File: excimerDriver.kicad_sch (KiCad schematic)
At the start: 37 parts, among them IC3 INA210, IC6 STM32G071KBT6, J1 B08B-XASK-1-A_LF__SN_, J2 TC2050-IDC, J3 BM02B-SRSS-TB_LF__SN_, J4 BM02B-SRSS-TB_LF__SN_, J6 640445-2, Q3 BSS138

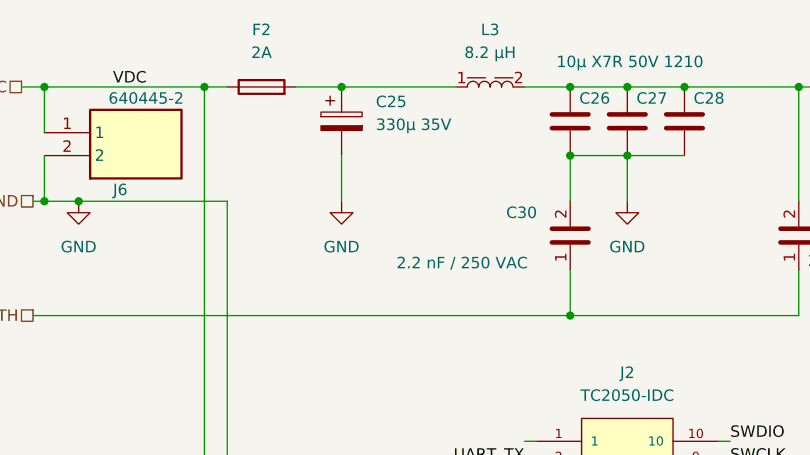
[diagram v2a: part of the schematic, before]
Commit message: branch main, transfomer changed to EF25
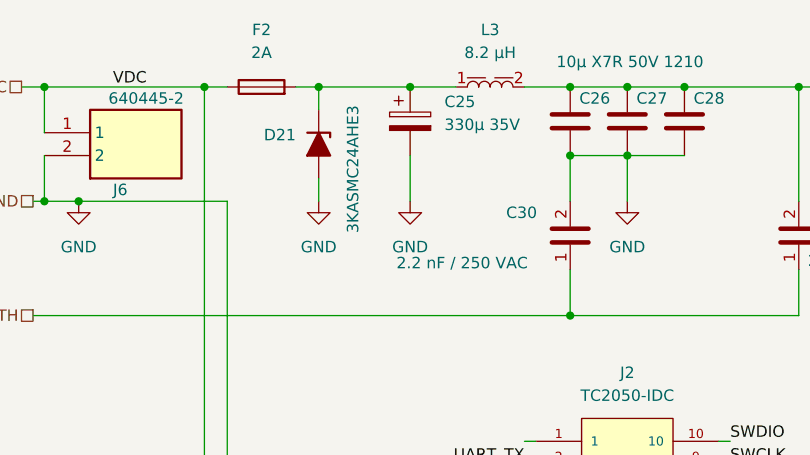
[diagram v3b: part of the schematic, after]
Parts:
- added D21: 3KASMC24AHE3, Diode_SMD:D_SMC, symbol Device:D_Zener_Filled
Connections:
- net GND: now also D21.2 (A)
- net at C25.1, F2.2, L3.1: now also D21.1 (K)
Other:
- moved on the sheet: C25
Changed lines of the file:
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@@
 	)
 	(junction
-		(at 57.15 25.4)
-		(diameter 0)
-		(color 0 0 0 0)
-	)
-	(junction
 		(at 107.95 25.4)
 		(diameter 0)
@@
 	)
 	(junction
+		(at 54.61 25.4)
+		(diameter 0)
+		(color 0 0 0 0)
+	)
+	(junction
+		(at 64.77 25.4)
+		(diameter 0)
+		(color 0 0 0 0)
+	)
+	(junction
 		(at 82.55 50.8)
 		(diameter 0)
@@
 	(wire
 		(pts
+			(xy 54.61 25.4) (xy 64.77 25.4)
+		)
+		(stroke
+			(width 0)
+			(type default)
+		)
+	)
+	(wire
+		(pts
 			(xy 236.22 130.81) (xy 223.52 130.81)
 		)
@@
 	(wire
 		(pts
-			(xy 52.07 25.4) (xy 57.15 25.4)
+			(xy 52.07 25.4) (xy 54.61 25.4)
 		)
 		(stroke
@@
 	(wire
 		(pts
+			(xy 54.61 25.4) (xy 54.61 27.94)
+		)
+		(stroke
+			(width 0)
+			(type default)
+		)
+	)
+	(wire
+		(pts
 			(xy 157.48 130.81) (xy 161.29 130.81)
 		)
@@
 	(wire
 		(pts
-			(xy 57.15 25.4) (xy 69.85 25.4)
+			(xy 99.06 67.31) (xy 116.84 67.31)
 		)
 		(stroke
@@
 	(wire
 		(pts
-			(xy 99.06 67.31) (xy 116.84 67.31)
+			(xy 95.25 101.6) (xy 95.25 104.14)
 		)
 		(stroke
@@
 	(wire
 		(pts
-			(xy 95.25 101.6) (xy 95.25 104.14)
+			(xy 31.75 132.08) (xy 48.26 132.08)
 		)
 		(stroke
@@
 	(wire
 		(pts
-			(xy 31.75 132.08) (xy 48.26 132.08)
+			(xy 107.95 38.1) (xy 107.95 25.4)
 		)
 		(stroke
@@
 	(wire
 		(pts
-			(xy 107.95 38.1) (xy 107.95 25.4)
+			(xy 64.77 25.4) (xy 69.85 25.4)
 		)
 		(stroke
@@
 	(wire
 		(pts
-			(xy 57.15 38.1) (xy 57.15 33.02)
+			(xy 64.77 33.02) (xy 64.77 38.1)
 		)
 		(stroke
@@
 	(wire
 		(pts
+			(xy 54.61 35.56) (xy 54.61 38.1)
+		)
+		(stroke
+			(width 0)
+			(type default)
+		)
+	)
+	(wire
+		(pts
 			(xy 48.26 132.08) (xy 48.26 114.3)
 		)
@@
 			"AAD4/////////yhzMtMiAQAA+P////////8EAAAAIgEAAPj/////////BAAAACIBAAD4////////"
 			"/yhzMtMiAQAA+P////////8EAAAAIgEAAPj/////////KHMy0yIBAAD4/////////yhzMtMiAQAA"
-			"+P////////8EAAAAIgEAAA=="
+			"+P////////8EAAAAIgEAAGaKDD5DdIJB3WLewGaKDD4AAACAAAAAAAAAgL8AAAAAAAAAAAAAAAAA"
+			"AAAAAAAAAAAAAAD///////////////8AAAAAAAAAgGaKDD4CAAAA5TYdQI+ERMAAAACA5TYdwAAA"
+			"AAAAAAAAe/I+Fd4MAYDgjqtF/n8AADsPhUECXNHAZYoMPhmwhkHLbdDAZ4oMPqrfhUHm5NDAZooM"
+			"PgUAAAAgJvNF/n8AACBwzrXeAQAAAAAAAN4BAAA+/FYnLr07swAAgL/trYknLr07swAAgL/trYkn"
+			"Lr07swAAgL8YsIZBzG3QwGaKDD48D4VBzG3QwGaKDD48D4VBAVzRwGaKDD4AAACAAAAAAP//f78A"
+			"AAAAAAAAAAAAAAAAAAAAAAAAAAAAAAD///////////////8AAAAAAAAAgGaKDD4CAAAAno8JQrQ2"
+			"ncAAAACAno8JwsB5EfveAQAACvJNFd4NAYDgjqtF/n8AAEJ0gkHeYt7AZYoMPj0PhUEAXNHAZ4oM"
+			"PsDBg0Fv39fAZooMPgUAAAAgJvNF/n8AACBwzrXeAQAAAAAAAAAAAADtrYknLr07swAAgL9JbIkn"
+			"Lr07swAAgL9NTIonLr07swAAgL88D4VBAVzRwGaKDD5DdIJB3WLewGaKDD48D4VB3WLewGaKDD4A"
+			"AAAAAAAAgAAAgL8AAAAAAAAAAAAAAAAAAAAAAAAAAAAAAAD///////////////8AAACAAAAAAGaK"
+			"DD4CAAAAAAAAgI+ERMCPhERA5TYdwAAAAAAAAAAAGfJcFQAOAYDgjqtF/n8AAGDEfkECXNHAp8y5"
+			"PfKCf0HLbdDAZ4oMPqkjf0Hm5NDAunDpPQUAAAAgJvNF/n8AACBwzrXeAQAAAAAAAN4BAADzBDU/"
+			"YsAEM/MENb/zBDU/Y8AEM/MENb/zBDU/YsAEM/MENb/xgn9BzG3QwGaKDD5hxH5BzG3QwKjMuT1h"
+			"xH5BAVzRwKjMuT0VBTU/AAAAANEENb8AAAAAAAAAAAAAAAAAAAAAAAAAAAAAAAD/////////////"
+			"//8AAAAAn/9/v8lQfUEAAAAA/vOrwZ6PCUKejwnCAAAAgOB5EfveAQAAKPJjFd4PAYDgjqtF/n8A"
+			"AGDEfkECXNHAp8y5PfKCf0HLbdDAZ4oMPqkjf0Hm5NDAunDpPQUAAAAgJvNF/n8AACBwzrXeAQAA"
+			"AAAAAAAAAADzBDU/YsAEM/MENb/zBDU/YsAEM/MENb/zBDU/YsAEM/MENb/xgn9BzG3QwGaKDD5h"
+			"xH5BAVzRwKjMuT3xgn9BAVzRwGaKDD4VBTU/AAAAANEENb8AAAAAAAAAAAAAAAAAAAAAAAAAAAAA"
+			"AAD///////////////8AAAAAAAAAAAAAAAAAAAAAAAAAAAAAAAAAAAAAAAAAAAAAAAAAAAAAAAAA"
+			"AAAAAAAAAAAAAAAAAAAAAAAAAAAAAAAAAAAAAAAAAAAAAAAAAAAAAAAAAAAAAAAAAAAAAAAAAAAA"
+			"AAAAAAAAAAAAAAAAAAAAAAAAAAAAAAAAAAAAAAAAAAAAAAAAAAAAAAAAAAAAAAAAAAAAAAAAAAAA"
+			"AAAAAAAAAAAAAAAAAAAAAAAAAAAAAAAAAAAAAAAAAAAAAAAAAAAAAAAAAAAAAAAAAAAAAAAAAAAA"
+			"AAAAAAAAAAAAAAAAAAAAAAAAAAAAAAAAAAAAAAAAAAAAAAAAAAAAAAAAAAAAAAAAAAAAAAAAAAAA"
+			"AAAAAAAAAAAAAAAAAAAAAAAAAAAAAAAAAAAAAAAAAAAAAAAAAAAAAAAAAAAAAAAAAAAAAAAAAAAA"
+			"AAAAAAAAAAAAAAAAAAAAAAAAAAAAAAAAAAAAAAAAAAAAAAAAAAAAAAAAAAAAAAAAAAAAAAAAAAAA"
+			"AAAAAAAAAAAAAAAAAAAAAAAAAAAAAAAAAAAAAAAAAAAAAAAAAAAAAAAAAAAAAAAAAAAAAAAAAAAA"
+			"AAAAAAAAAAAAAAAAAAAAAAAAAAAAAAAAAAAAAAAAAAAAAAAAAAAAAAAAAAAAAAAAAAAAAAAAAAAA"
+			"AAAAAAAAAAAAAAAAAAAAAAAAAAAAAAAAAAAAAAAAAAAAAAAAAAAAAAAAAAAAAAAAAAAAAAAAAAAA"
+			"AAAAAAAAAAAAAAAAAAAAAAAAAAAAAAAAAAAAAAAAAAAAAAAAAAAAAAAAAAAAAAAAAAAAAAAAAAAA"
+			"AAAAAAAAAAAAAAAAAAAAAAAAAAAAAAAAAAAAAAAAAAAAAAAAAAAAAAAAAAAAAAAAAAAAAAAAAAAA"
+			"AAAAAAAAAAAAAAAAAAAAAAAAAAAAAAAAAAAAAAAAAAAAAAAAAAAAAAAAAAAAAAAAAAAAAAAAAAAA"
+			"AAAAAAAAAAAAAAAAAAAAAAAAAAAAAAAAAAAAAAAAAAAAAAAAAAAAAAAAAAAAAAAAAAAAAAAAAAAA"
+			"AAAAAAAAAAAAAAAAAAAAAAAAAAAAAAAAAAAAAAAAAAAAAAAAAAAAAAAAAAAAAAAAAAAAAAAAAAAA"
+			"AAAAAAAAAAAAAAAAAAAAAAAAAAAAAAAAAAAAAAAAAAAAAAAAAAAAAAAAAAAAAAAAAAAAAAAAAAAA"
+			"AAAAAAAAAAAAAAAAAAAAAAAAAAAAAAAAAAAAAAAAAAAAAAAAAAAAAAAAAAAAAAAAAAAAAAAAAAAA"
+			"AAAAAAAAAAAAAAAAAAAAAAAAAAAAAAAAAAAAAAAAAAAAAAAAAAAAAAAAAAAAAAAAAAAAAAAAAAAA"
+			"AAAAAAAAAAAAAAAAAAAAAA=="
 		)
 	)
@@
 	(symbol
 		(lib_id "power:GND")
-		(at 57.15 38.1 0)
+		(at 64.77 38.1 0)
 		(unit 1)
 		(exclude_from_sim no)
@@
 		(fields_autoplaced yes)
 		(property "Reference" "#PWR023"
-			(at 57.15 44.45 0)
+			(at 64.77 44.45 0)
 			(hide yes)
 			(effects
@@
 		)
 		(property "Value" "GND"
-			(at 57.15 43.18 0)
+			(at 64.77 43.18 0)
 			(effects
 				(font
@@
 		)
 		(property "Footprint" ""
-			(at 57.15 38.1 0)
+			(at 64.77 38.1 0)
 			(hide yes)
 			(effects
@@
 		)
 		(property "Datasheet" ""
-			(at 57.15 38.1 0)
+			(at 64.77 38.1 0)
 			(hide yes)
 			(effects
@@
 		)
 		(property "Description" "Power symbol creates a global label with name \"GND\" , ground"
-			(at 57.15 38.1 0)
+			(at 64.77 38.1 0)
 			(hide yes)
 			(effects
@@
 	(symbol
 		(lib_id "Device:C_Polarized")
-		(at 57.15 29.21 0)
+		(at 64.77 29.21 0)
 		(unit 1)
 		(exclude_from_sim no)
@@
 		(fields_autoplaced yes)
 		(property "Reference" "C25"
-			(at 60.96 27.0509 0)
+			(at 68.58 27.0509 0)
 			(effects
 				(font
@@
 		)
 		(property "Value" "330µ 35V"
-			(at 60.96 29.5909 0)
+			(at 68.58 29.5909 0)
 			(effects
 				(font
@@
 		)
 		(property "Footprint" "Capacitor_THT:CP_Radial_D13.0mm_P5.00mm"
-			(at 58.1152 33.02 0)
+			(at 65.7352 33.02 0)
 			(hide yes)
 			(effects
@@
 		)
 		(property "Datasheet" ""
-			(at 57.15 29.21 0)
+			(at 64.77 29.21 0)
 			(hide yes)
 			(effects
@@
 		)
 		(property "Description" "Polarized capacitor"
-			(at 57.15 29.21 0)
+			(at 64.77 29.21 0)
 			(hide yes)
 			(effects
@@
 	)
 	(symbol
+		(lib_id "power:GND")
+		(at 54.61 38.1 0)
+		(unit 1)
+		(exclude_from_sim no)
+		(in_bom yes)
+		(on_board yes)
+		(dnp no)
+		(fields_autoplaced yes)
+		(property "Reference" "#PWR074"
+			(at 54.61 44.45 0)
+			(hide yes)
+			(effects
+				(font
+					(size 1.27 1.27)
+				)
+			)
+		)
+		(property "Value" "GND"
+			(at 54.61 43.18 0)
+			(effects
+				(font
+					(size 1.27 1.27)
+				)
+			)
+		)
+		(property "Footprint" ""
+			(at 54.61 38.1 0)
+			(hide yes)
+			(effects
+				(font
+					(size 1.27 1.27)
+				)
+			)
+		)
+		(property "Datasheet" ""
+			(at 54.61 38.1 0)
+			(hide yes)
+			(effects
+				(font
+					(size 1.27 1.27)
+				)
+			)
+		)
+		(property "Description" "Power symbol creates a global label with name \"GND\" , ground"
+			(at 54.61 38.1 0)
+			(hide yes)
+			(effects
+				(font
+					(size 1.27 1.27)
+				)
+			)
+		)
+		(pin "1"
+		)
+		(instances
+			(project "OSLUV"
+				(path "/c6e900e0-9399-44f0-8089-9dd7b8ffe54c/9b3070c3-43e0-4d43-9da1-9bc1bd2d6fb9"
+					(reference "#PWR074")
+					(unit 1)
+				)
+			)
+		)
+	)
+	(symbol
 		(lib_id "Device:R")
 		(at 241.3 41.91 180)
@@
 					(unit 1)
 				)
+			)
+		)
+	)
+	(symbol
+		(lib_id "Device:D_Zener_Filled")
+		(at 54.61 31.75 270)
+		(unit 1)
+		(exclude_from_sim no)
+		(in_bom yes)
+		(on_board yes)
+		(dnp no)
+		(property "Reference" "D21"
+			(at 48.514 30.734 90)
+			(effects
+				(font
+					(size 1.27 1.27)
+				)
+				(justify left)
+			)
+		)
+		(property "Value" "3KASMC24AHE3"
+			(at 58.42 27.432 0)
+			(effects
+				(font
+					(size 1.27 1.27)
+				)
+				(justify left)
+			)
+		)
+		(property "Footprint" "Diode_SMD:D_SMC"
+			(at 54.61 31.75 0)
+			(hide yes)
+			(effects
+				(font
+					(size 1.27 1.27)
+				)
+			)
+		)
+		(property "Datasheet" ""
+			(at 54.61 31.75 0)
+			(hide yes)
+			(effects
+				(font
+					(size 1.27 1.27)
+				)
+			)
+		)
+		(property "Description" "Zener diode, filled shape"
+			(at 54.61 31.75 0)
+			(hide yes)
+			(effects
+				(font
+					(size 1.27 1.27)
+				)
+			)
+		)
+		(pin "1"
+		)
+		(pin "2"
+		)
+		(instances
+			(project ""
+				(path "/c6e900e0-9399-44f0-8089-9dd7b8ffe54c/9b3070c3-43e0-4d43-9da1-9bc1bd2d6fb9"
+					(reference "D21")
+					(unit 1)
+				)

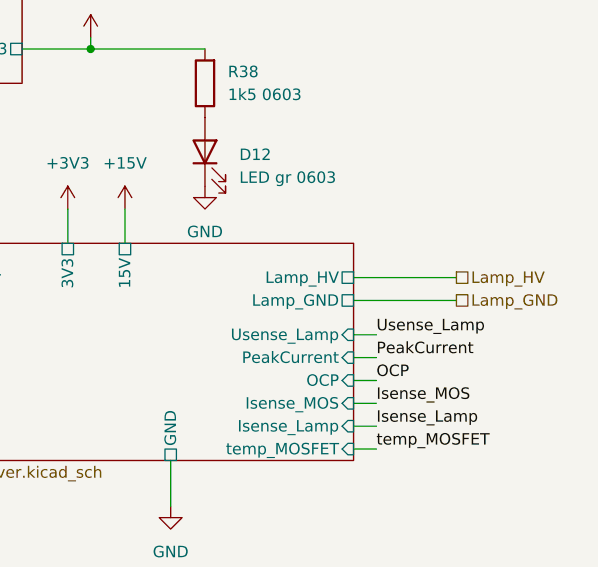
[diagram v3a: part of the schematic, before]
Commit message: new transformer, top layer only
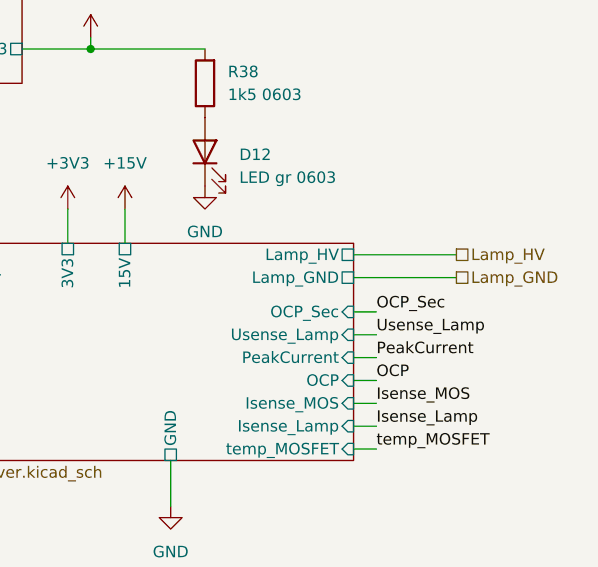
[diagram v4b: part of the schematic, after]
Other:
- sheet lampDriver ports: added OCP_Sec; removed none
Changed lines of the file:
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@@
 	(wire
 		(pts
-			(xy 257.81 63.5) (xy 269.24 63.5)
+			(xy 257.81 60.96) (xy 269.24 60.96)
 		)
 		(stroke
@@
 	(wire
 		(pts
+			(xy 257.81 67.31) (xy 260.35 67.31)
+		)
+		(stroke
+			(width 0)
+			(type default)
+		)
+	)
+	(wire
+		(pts
 			(xy 95.25 101.6) (xy 95.25 104.14)
 		)
@@
 	(wire
 		(pts
-			(xy 257.81 66.04) (xy 269.24 66.04)
+			(xy 257.81 63.5) (xy 269.24 63.5)
 		)
 		(stroke
@@
 			"AAAAAAAAAAAAAAAAAAAAAAAAAAAAAAAAAAAAAAAAAAAAAAAAAAAAAAAAAAAAAAAAAAAAAAAAAAAA"
 			"AAAAAAAAAAAAAAAAAAAAAAAAAAAAAAAAAAAAAAAAAAAAAAAAAAAAAAAAAAAAAAAAAAAAAAAAAAAA"
+			"AAAAAAAAAAAAAAAAAAAAAAAAAAAAAAAAAAAAAAAAAAAAAAAAAAAAAAAAAAAAAAAAAAAAAAAAAAAA"
+			"AAAAAAAAAAAAAAAAAAAAAAAAAAAAAAAAAAAAAAAAAAAAAAAAAAAAAAAAAAAAAAAAAAAAAAAAAAAA"
+			"AAAAAAAAAAAAAAAAAAAAAAAAAAAAAAAAAAAAAAAAAAAAAAAAAAAAAAAAAAAAAAAAAAAAAAAAAAAA"
+			"AAAAAAAAAAAAAAAAAAAAAAAAAAAAAAAAAAAAAAAAAAAAAAAAAAAAAAAAAAAAAAAAAAAAAAAAAAAA"
+			"AAAAAAAAAAAAAAAAAAAAAAAAAAAAAAAAAAAAAAAAAAAAAAAAAAAAAAAAAAAAAAAAAAAAAAAAAAAA"
+			"AAAAAAAAAAAAAAAAAAAAAAAAAAAAAAAAAAAAAAAAAAAAAAAAAAAAAAAAAAAAAAAAAAAAAAAAAAAA"
+			"AAAAAAAAAAAAAAAAAAAAAAAAAAAAAAAAAAAAAAAAAAAAAAAAAAAAAAAAAAAAAAAAAAAAAAAAAAAA"
+			"AAAAAAAAAAAAAAAAAAAAAAAAAAAAAAAAAAAAAAAAAAAAAAAAAAAAAAAAAAAAAAAAAAAAAAAAAAAA"
+			"AAAAAAAAAAAAAAAAAAAAAAAAAAAAAAAAAAAAAAAAAAAAAAAAAAAAAAAAAAAAAAAAAAAAAAAAAAAA"
+			"AAAAAAAAAAAAAAAAAAAAAAAAAAAAAAAAAAAAAAAAAAAAAAAAAAAAAAAAAAAAAAAAAAAAAAAAAAAA"
+			"AAAAAAAAAAAAAAAAAAAAAAAAAAAAAAAAAAAAAAAAAAAAAAAAAAAAAAAAAAAAAAAAAAAAAAAAAAAA"
+			"AAAAAAAAAAAAAAAAAAAAAAAAAAAAAAAAAAAAAAAAAAAAAAAAAAAAAAAAAAAAAAAAAAAAAAAAAAAA"
+			"AAAAAAAAAAAAAAAAAAAAAAAAAAAAAAAAAAAAAAAAAAAAAAAAAAAAAAAAAAAAAAAAAAAAAAAAAAAA"
+			"AAAAAAAAAAAAAAAAAAAAAAAAAAAAAAAAAAAAAAAAAAAAAAAAAAAAAAAAAAAAAAAAAAAAAAAAAAAA"
+			"AAAAAAAAAAAAAAAAAAAAAAAAAAAAAAAAAAAAAAAAAAAAAAAAAAAAAAAAAAAAAAAAAAAAAAAAAAAA"
+			"AAAAAAAAAAAAAAAAAAAAAAAAAAAAAAAAAAAAAAAAAAAAAAAAAAAAAAAAAAAAAAAAAAAAAAAAAAAA"
+			"AAAAAAAAAAAAAAAAAAAAAAAAAAAAAAAAAAAAAAAAAAAAAAAAAAAAAAAAAAAAAAAAAAAAAAAAAAAA"
+			"AAAAAAAAAAAAAAAAAAAAAAAAAAAAAAAAAAAAAAAAAAAAAAAAAAAAAAAAAAAAAAAAAAAAAAAAAAAA"
+			"AAAAAAAAAAAAAAAAAAAAAAAAAAAAAAAAAAAAAAAAAAAAAAAAAAAAAAAAAAAAAAAAAAAAAAAAAAAA"
+			"AAAAAAAAAAAAAAAAAAAAAAAAAAAAAAAAAAAAAAAAAAAAAAAAAAAAAAAAAAAAAAAAAAAAAAAAAAAA"
+			"AAAAAAAAAAAAAAAAAAAAAAAAAAAAAAAAAAAAAAAAAAAAAAAAAAAAAAAAAAAAAAAAAAAAAAAAAAAA"
+			"AAAAAAAAAAAAAAAAAAAAAAAAAAAAAAAAAAAAAAAAAAAAAAAAAAAAAAAAAAAAAAAAAAAAAAAAAAAA"
+			"AAAAAAAAAAAAAAAAAAAAAAAAAAAAAAAAAAAAAAAAAAAAAAAAAAAAAAAAAAAAAAAAAAAAAAAAAAAA"
+			"AAAAAAAAAAAAAAAAAAAAAAAAAAAAAAAAAAAAAAAAAAAAAAAAAAAAAAAAAAAAAAAAAAAAAAAAAAAA"
+			"AAAAAAAAAAAAAAAAAAAAAAAAAAAAAAAAAAAAAAAAAAAAAAAAAAAAAAAAAAAAAAAAAAAAAAAAAAAA"
+			"AAAAAAAAAAAAAAAAAAAAAAAAAAAAAAAAAAAAAAAAAAAAAAAAAAAAAAAAAAAAAAAAAAAAAAAAAAAA"
+			"AAAAAAAAAAAAAAAAAAAAAAAAAAAAAAAAAAAAAAAAAAAAAAAAAAAAAAAAAAAAAAAAAAAAAAAAAAAA"
+			"AAAAAAAAAAAAAAAAAAAAAAAAAAAAAAAAAAAAAAAAAAAAAAAAAAAAAAAAAAAAAAAAAAAAAAAAAAAA"
+			"AAAAAAAAAAAAAAAAAAAAAAAAAAAAAAAAAAAAAAAAAAAAAAAAAAAAAAAAAAAAAAAAAAAAAAAAAAAA"
+			"AAAAAAAAAAAAAAAAAAAAAAAAAAAAAAAAAAAAAAAAAAAAAAAAAAAAAAAAAAAAAAAAAAAAAAAAAAAA"
+			"AAAAAAAAAAAAAAAAAAAAAAAAAAAAAAAAAAAAAAAAAAAAAAAAAAAAAAAAAAAAAAAAAAAAAAAAAAAA"
+			"AAAAAAAAAAAAAAAAAAAAAAAAAAAAAAAAAAAAAAAAAAAAAAAAAAAAAAAAAAAAAAAAAAAAAAAAAAAA"
+			"AAAAAAAAAAAAAAAAAAAAAAAAAAAAAAAAAAAAAAAAAAAAAAAAAAAAAAAAAAAAAAAAAAAAAAAAAAAA"
+			"AAAAAAAAAAAAAAAAAAAAAAAAAAAAAAAAAAAAAAAAAAAAAAAAAAAAAAAAAAAAAAAAAAAAAAAAAAAA"
+			"AAAAAAAAAAAAAAAAAAAAAAAAAAAAAAAAAAAAAAAAAAAAAAAAAAAAAAAAAAAAAAAAAAAAAAAAAAAA"
+			"AAAAAAAAAAAAAAAAAAAAAAAAAAAAAAAAAAAAAAAAAAAAAAAAAAAAAAAAAAAAAAAAAAAAAAAAAAAA"
+			"AAAAAAAAAAAAAAAAAAAAAAAAAAAAAAAAAAAAAAAAAAAAAAAAAAAAAAAAAAAAAAAAAAAAAAAAAAAA"
+			"AAAAAAAAAAAAAAAAAAAAAAAAAAAAAAAAAAAAAAAAAAAAAAAAAAAAAAAAAAAAAAAAAAAAAAAAAAAA"
+			"AAAAAAAAAAAAAAAAAAAAAAAAAAAAAAAAAAAAAAAAAAAAAAAAAAAAAAAAAAAAAAAAAAAAAAAAAAAA"
+			"AAAAAAAAAAAAAAAAAAAAAAAAAAAAAAAAAAAAAAAAAAAAAAAAAAAAAAAAAAAAAAAAAAAAAAAAAAAA"
+			"AAAAAAAAAAAAAAAAAAAAAAAAAAAAAAAAAAAAAAAAAAAAAAAAAAAAAAAAAAAAAAAAAAAAAAAAAAAA"
+			"AAAAAAAAAAAAAAAAAAAAAAAAAAAAAAAAAAAAAAAAAAAAAAAAAAAAAAAAAAAAAAAAAAAAAAAAAAAA"
+			"AAAAAAAAAAAAAAAAAAAAAAAAAAAAAAAAAAAAAAAAAAAAAAAAAAAAAAAAAAAAAAAAAAAAAAAAAAAA"
+			"AAAAAAAAAAAAAAAAAAAAAAAAAAAAAAAAAAAAAAAAAAAAAAAAAAAAAAAAAAAAAAAAAAAAAAAAAAAA"
+			"AAAAAAAAAAAAAAAAAAAAAAAAAAAAAAAAAAAAAAAAAAAAAAAAAAAAAAAAAAAAAAAAAAAAAAAAAAAA"
+			"AAAAAAAAAAAAAAAAAAAAAAAAAAAAAAAAAAAAAAAAAAAAAAAAAAAAAAAAAAAAAAAAAAAAAAAAAAAA"
+			"AAAAAAAAAAAAAAAAAAAAAAAAAAAAAAAAAAAAAAAAAAAAAAAAAAAAAAAAAAAAAAAAAAAAAAAAAAAA"
+			"AAAAAAAAAAAAAAAAAAAAAAAAAAAAAAAAAAAAAAAAAAAAAAAAAAAAAAAAAAAAAAAAAAAAAAAAAAAA"
+			"AAAAAAAAAAAAAAAAAAAAAAAAAAAAAAAAAAAAAAAAAAAAAAAAAAAAAAAAAAAAAAAAAAAAAAAAAAAA"
+			"AAAAAAAAAAAAAAAAAAAAAAAAAAAAAAAAAAAAAAAAAAAAAAAAAAAAAAAAAAAAAAAAAAAAAAAAAAAA"
+			"AAAAAAAAAAAAAAAAAAAAAAAAAAAAAAAAAAAAAAAAAAAAAAAAAAAAAAAAAAAAAAAAAAAAAAAAAAAA"
+			"AAAAAAAAAAAAAAAAAAAAAAAAAAAAAAAAAAAAAAAAAAAAAAAAAAAAAAAAAAAAAAAAAAAAAAAAAAAA"
+			"AAAAAAAAAAAAAAAAAAAAAAAAAAAAAAAAAAAAAAAAAAAAAAAAAAAAAAAAAAAAAAAAAAAAAAAAAAAA"
+			"AAAAAAAAAAAAAAAAAAAAAAAAAAAAAAAAAAAAAAAAAAAAAAAAAAAAAAAAAAAAAAAAAAAAAAAAAAAA"
 			"AAAAAAAAAAAAAAAAAAAAAA=="
 		)
@@
 		)
 	)
+	(label "OCP_Sec"
+		(at 260.35 67.31 0)
+		(effects
+			(font
+				(size 1.27 1.27)
+			)
+			(justify left bottom)
+		)
+	)
 	(label "PeakCurrent"
 		(at 123.19 132.08 0)
@@
 	(hierarchical_label "Lamp_GND"
 		(shape passive)
-		(at 269.24 66.04 0)
+		(at 269.24 63.5 0)
 		(effects
 			(font
@@
 	(hierarchical_label "Lamp_HV"
 		(shape passive)
-		(at 269.24 63.5 0)
+		(at 269.24 60.96 0)
 		(effects
 			(font
@@
 		)
 		(pin "Lamp_HV" passive
-			(at 257.81 63.5 0)
+			(at 257.81 60.96 0)
 			(effects
 				(font
@@
 		)
 		(pin "Lamp_GND" passive
-			(at 257.81 66.04 0)
+			(at 257.81 63.5 0)
 			(effects
 				(font
@@
 			)
 		)
+		(pin "OCP_Sec" input
+			(at 257.81 67.31 0)
+			(effects
+				(font
+					(size 1.27 1.27)
+				)
+				(justify right)
+			)
+		)
